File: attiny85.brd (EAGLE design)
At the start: 88.3 x 50.2 mm, 9 parts, among them U2 ATTINY85V-10SU

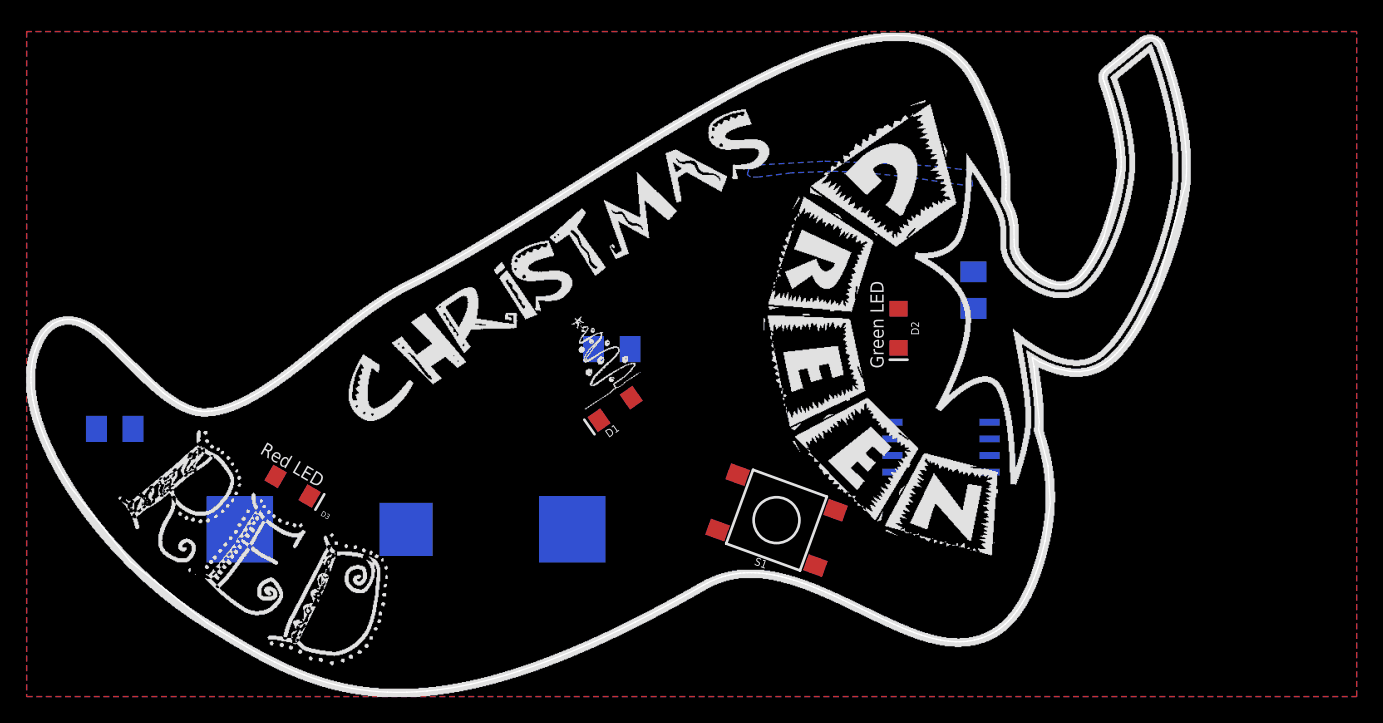
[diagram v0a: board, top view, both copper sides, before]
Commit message: Updating pads and rerouting
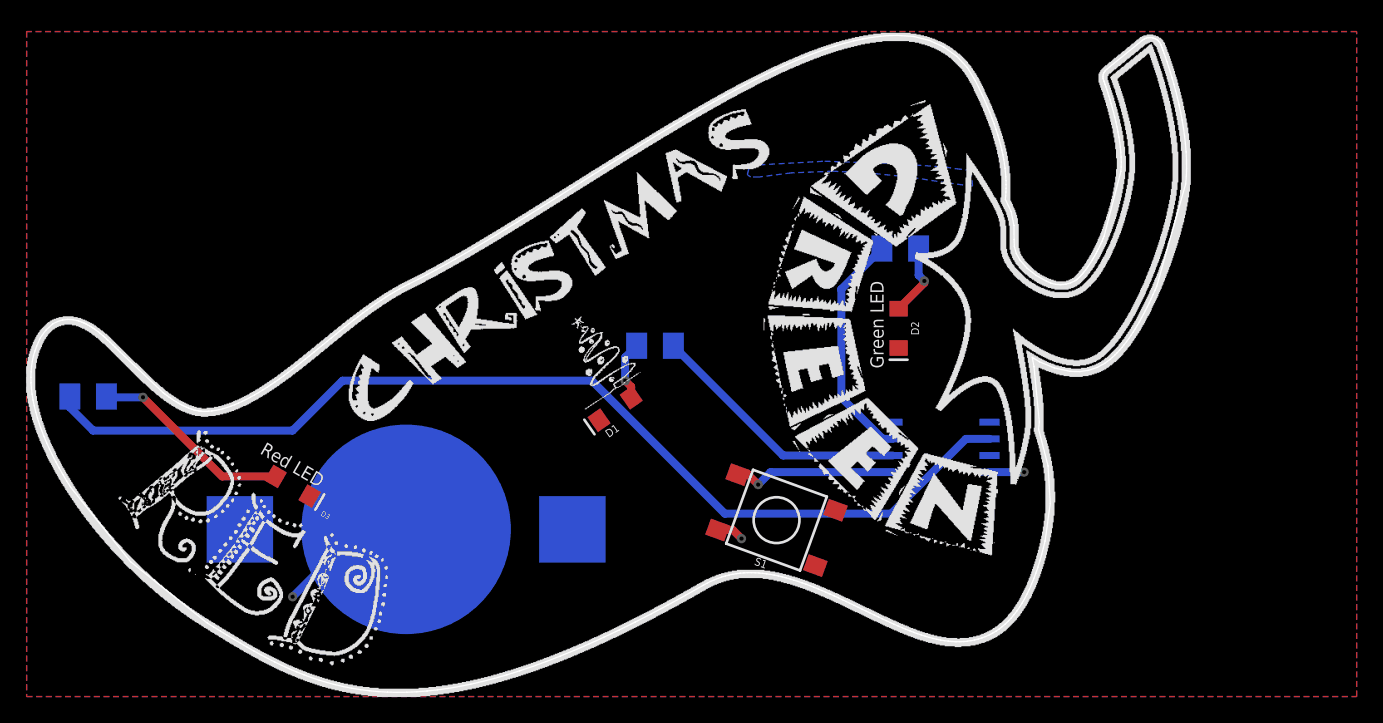
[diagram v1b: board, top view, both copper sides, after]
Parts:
- BAT1: device adafruit:CR2032-SMD -> adafruit-john modded:CR2032-SMD
- moved R2 6.43 mm to (66.7, 34.2), turned to 180 degrees
- moved R1 3.31 mm to (48.0, 26.8), turned to 0 degrees
- moved R3 3.20 mm to (4.70, 22.9)
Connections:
- removed net N$3: BAT1.+$1, BAT1.+$2, S1.B2, U2.8
- new net VCC: BAT1.+$1, BAT1.+$2, S1.B2, U2.8
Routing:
- net N$8: track 0.00 -> 80.0 mm
- net N$4: track 0.00 -> 20.2 mm
- net N$7: track 0.00 -> 17.9 mm
- net N$1: track 0.00 -> 15.5 mm, vias 0 -> 1
- net GND: track 0.00 -> 13.4 mm, vias 0 -> 2
- net N$6: track 0.00 -> 12.5 mm, vias 0 -> 1
- net N$2: track 0.00 -> 5.59 mm, vias 0 -> 1
- net N$5: track 0.00 -> 4.53 mm, vias 0 -> 1
- net VCC: track 0.00 -> 2.10 mm, vias 0 -> 1
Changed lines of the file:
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@@
 <setting verticaltext="up"/>
 </settings>
-<grid distance="0.0025" unitdist="inch" unit="inch" style="lines" multiple="1" display="yes" altdistance="0.0125" altunitdist="inch" altunit="inch"/>
+<grid distance="0.05" unitdist="inch" unit="inch" style="lines" multiple="1" display="yes" altdistance="0.0125" altunitdist="inch" altunit="inch"/>
 <layers>
 <layer number="1" name="Top" color="4" fill="1" visible="yes" active="yes"/>
@@
 </autorouter>
 <elements>
-<element name="R2" library="adafruit" package="M1206" value="1k" x="72.3265" y="31.0515" rot="MR270"/>
+<element name="R2" library="adafruit" package="M1206" value="1k" x="66.7385" y="34.2265" rot="MR180"/>
 <element name="D2" library="SparkFun-LED" package="LED-1206" value="" x="66.6115" y="28.1305" rot="R270"/>
-<element name="R3" library="adafruit" package="M1206" value="1k" x="6.731" y="20.447" rot="MR180"/>
+<element name="R3" library="adafruit" package="M1206" value="1k" x="4.699" y="22.9235" rot="MR180"/>
 <element name="D3" library="SparkFun-LED" package="LED-1206" value="" x="20.32" y="16.0655" smashed="yes" rot="R330">
 <attribute name="NAME" x="22.41786875" y="13.85710625" size="0.4064" layer="25" ratio="10" rot="R330"/>
 <attribute name="VALUE" x="22.1899375" y="12.90351875" size="1.27" layer="27" ratio="10" rot="R330"/>
 </element>
-<element name="BAT1" library="adafruit" package="CR2032-SMD" value="" x="28.9885" y="12.7725" rot="MR0"/>
+<element name="BAT1" library="adafruit-john modded" package="CR2032-SMD" value="" x="28.9885" y="12.7725" rot="MR0"/>
 <element name="U2" library="Atmel_By_element14_Batch_1-00" package="SOIC127P798X216-8N" value="ATTINY85V-10SU" x="69.85" y="19.05" smashed="yes" rot="MR0">
 <attribute name="OC_NEWARK" value="58M3799" x="69.85" y="19.05" size="1.778" layer="28" rot="MR0" display="off"/>
@@
 <attribute name="NAME" x="74.4728" y="13.7922" size="2.0828" layer="26" ratio="10" rot="SMR0"/>
 </element>
-<element name="R1" library="adafruit" package="M1206" value="1k" x="44.704" y="26.543" rot="MR180"/>
+<element name="R1" library="adafruit" package="M1206" value="1k" x="48.006" y="26.797" rot="MR0"/>
 <element name="D1" library="SparkFun-LED" package="LED-1206" value="" x="44.958" y="21.971" smashed="yes" rot="R215">
 <attribute name="NAME" x="44.55183125" y="20.55575625" size="0.6096" layer="25" font="vector" ratio="20" rot="R215" align="bottom-center"/>
@@
 <contactref element="R2" pad="2"/>
 <contactref element="D2" pad="A"/>
-<wire x1="66.6115" y1="29.6305" x2="72.3265" y2="29.6515" width="0" layer="19" extent="1-16"/>
+<wire x1="66.6115" y1="29.6305" x2="68.58" y2="31.599" width="0.6096" layer="1"/>
+<wire x1="68.58" y1="31.599" x2="68.58" y2="31.75" width="0.6096" layer="1"/>
+<via x="68.58" y="31.75" extent="1-16" drill="0.3048"/>
+<wire x1="68.58" y1="31.75" x2="68.1385" y2="32.1915" width="0.6096" layer="16"/>
+<wire x1="68.1385" y1="32.1915" x2="68.1385" y2="34.2265" width="0.6096" layer="16"/>
 </signal>
 <signal name="VCC">
@@
 <vertex x="0" y="50.8"/>
 </polygon>
+<contactref element="BAT1" pad="+$1"/>
+<contactref element="BAT1" pad="+$2"/>
+<contactref element="U2" pad="8"/>
+<contactref element="S1" pad="B2"/>
+<wire x1="52.781228125" y1="12.72185" x2="53.95315" y2="12.72185" width="0.6096" layer="1"/>
+<wire x1="53.95315" y1="12.72185" x2="54.61" y2="12.065" width="0.6096" layer="1"/>
+<via x="54.61" y="12.065" extent="1-16" drill="0.3048"/>
 </signal>
 <signal name="GND">
@@
 <contactref element="D3" pad="C"/>
 <contactref element="D2" pad="C"/>
-<wire x1="73.5584" y1="17.145" x2="66.6115" y2="26.6305" width="0" layer="19" extent="1-16"/>
-<wire x1="43.729271875" y1="21.110634375" x2="66.6115" y2="26.6305" width="0" layer="19" extent="1-1"/>
-<wire x1="28.9885" y1="12.7725" x2="43.729271875" y2="21.110634375" width="0" layer="19" extent="1-16"/>
-<wire x1="21.6190375" y1="15.3155" x2="28.9885" y2="12.7725" width="0" layer="19" extent="1-16"/>
+<wire x1="28.9885" y1="12.7725" x2="25.4725" y2="12.7725" width="0.6096" layer="16"/>
+<wire x1="25.4725" y1="12.7725" x2="20.32" y2="7.62" width="0.6096" layer="16"/>
+<via x="20.32" y="7.62" extent="1-16" drill="0.3048"/>
+<wire x1="73.5584" y1="17.145" x2="76.2" y2="17.145" width="0.6096" layer="16"/>
+<via x="76.2" y="17.145" extent="1-16" drill="0.3048"/>
 </signal>
 <signal name="N$1">
 <contactref element="R3" pad="2"/>
 <contactref element="D3" pad="A"/>
-<wire x1="8.131" y1="20.447" x2="19.020959375" y2="16.8155" width="0" layer="19" extent="1-16"/>
+<wire x1="19.020959375" y1="16.8155" x2="14.9345" y2="16.8155" width="0.6096" layer="1"/>
+<wire x1="14.9345" y1="16.8155" x2="8.89" y2="22.86" width="0.6096" layer="1"/>
+<via x="8.89" y="22.86" extent="1-16" drill="0.3048"/>
+<wire x1="8.89" y1="22.86" x2="6.1625" y2="22.86" width="0.6096" layer="16"/>
+<wire x1="6.1625" y1="22.86" x2="6.099" y2="22.9235" width="0.6096" layer="16"/>
 </signal>
 <signal name="N$5">
 <contactref element="R1" pad="2"/>
 <contactref element="D1" pad="A"/>
-<wire x1="46.186725" y1="22.8313625" x2="46.104" y2="26.543" width="0" layer="19" extent="1-16"/>
+<wire x1="46.606" y1="26.797" x2="45.72" y2="25.911" width="0.6096" layer="16"/>
+<wire x1="45.72" y1="25.911" x2="45.72" y2="24.13" width="0.6096" layer="16"/>
+<via x="45.72" y="24.13" extent="1-16" drill="0.3048"/>
+<wire x1="45.72" y1="24.13" x2="46.186725" y2="23.663275" width="0.6096" layer="1"/>
+<wire x1="46.186725" y1="23.663275" x2="46.186725" y2="22.8313625" width="0.6096" layer="1"/>
 </signal>
 <signal name="NTOUCH">
@@
 </polygon>
 </signal>
-<signal name="N$3">
-<contactref element="BAT1" pad="+$1"/>
-<contactref element="BAT1" pad="+$2"/>
-<contactref element="U2" pad="8"/>
-<contactref element="S1" pad="B2"/>
-<wire x1="52.781228125" y1="12.72185" x2="66.1416" y2="20.955" width="0" layer="19" extent="1-16"/>
-<wire x1="41.6885" y1="12.7725" x2="52.781228125" y2="12.72185" width="0" layer="19" extent="1-16"/>
-<wire x1="16.2885" y1="12.7725" x2="41.6885" y2="12.7725" width="0" layer="19" extent="16-16"/>
-</signal>
 <signal name="N$6">
 <contactref element="U2" pad="5"/>
 <contactref element="S1" pad="A2"/>
-<wire x1="54.32031875" y1="16.95046875" x2="66.1416" y2="17.145" width="0" layer="19" extent="1-16"/>
+<wire x1="66.1416" y1="17.145" x2="56.8325" y2="17.145" width="0.6096" layer="16"/>
+<wire x1="56.8325" y1="17.145" x2="55.88" y2="16.1925" width="0.6096" layer="16"/>
+<via x="55.88" y="16.1925" extent="1-16" drill="0.3048"/>
+<wire x1="55.88" y1="16.1925" x2="55.12203125" y2="16.95046875" width="0.6096" layer="1"/>
+<wire x1="55.12203125" y1="16.95046875" x2="54.32031875" y2="16.95046875" width="0.6096" layer="1"/>
 </signal>
 <signal name="N$4">
 <contactref element="U2" pad="6"/>
 <contactref element="R1" pad="1"/>
-<wire x1="43.304" y1="26.543" x2="66.1416" y2="18.415" width="0" layer="19" extent="16-16"/>
+<wire x1="49.406" y1="26.797" x2="57.788" y2="18.415" width="0.6096" layer="16"/>
+<wire x1="57.788" y1="18.415" x2="66.1416" y2="18.415" width="0.6096" layer="16"/>
 </signal>
 <signal name="N$7">
 <contactref element="U2" pad="7"/>
 <contactref element="R2" pad="1"/>
-<wire x1="66.1416" y1="19.685" x2="72.3265" y2="32.4515" width="0" layer="19" extent="16-16"/>
+<wire x1="65.3385" y1="34.2265" x2="62.23" y2="31.118" width="0.6096" layer="16"/>
+<wire x1="62.23" y1="31.118" x2="62.23" y2="22.86" width="0.6096" layer="16"/>
+<wire x1="62.23" y1="22.86" x2="65.405" y2="19.685" width="0.6096" layer="16"/>
+<wire x1="65.405" y1="19.685" x2="66.1416" y2="19.685" width="0.6096" layer="16"/>
 </signal>
 <signal name="N$8">
 <contactref element="U2" pad="2"/>
 <contactref element="R3" pad="1"/>
-<wire x1="5.331" y1="20.447" x2="73.5584" y2="19.685" width="0" layer="19" extent="16-16"/>
+<wire x1="3.299" y1="22.9235" x2="3.299" y2="22.101" width="0.6096" layer="16"/>
+<wire x1="3.299" y1="22.101" x2="5.08" y2="20.32" width="0.6096" layer="16"/>
+<wire x1="5.08" y1="20.32" x2="20.32" y2="20.32" width="0.6096" layer="16"/>
+<wire x1="20.32" y1="20.32" x2="24.13" y2="24.13" width="0.6096" layer="16"/>
+<wire x1="24.13" y1="24.13" x2="43.18" y2="24.13" width="0.6096" layer="16"/>
+<wire x1="43.18" y1="24.13" x2="53.34" y2="13.97" width="0.6096" layer="16"/>
+<wire x1="53.34" y1="13.97" x2="66.04" y2="13.97" width="0.6096" layer="16"/>
+<wire x1="66.04" y1="13.97" x2="71.755" y2="19.685" width="0.6096" layer="16"/>
+<wire x1="71.755" y1="19.685" x2="73.5584" y2="19.685" width="0.6096" layer="16"/>
 </signal>
 </signals>

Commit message: Updating the board and schematic
This is a fairly big set of changes based on the prototype, going
to run another round just to be sure since I've got enough time.
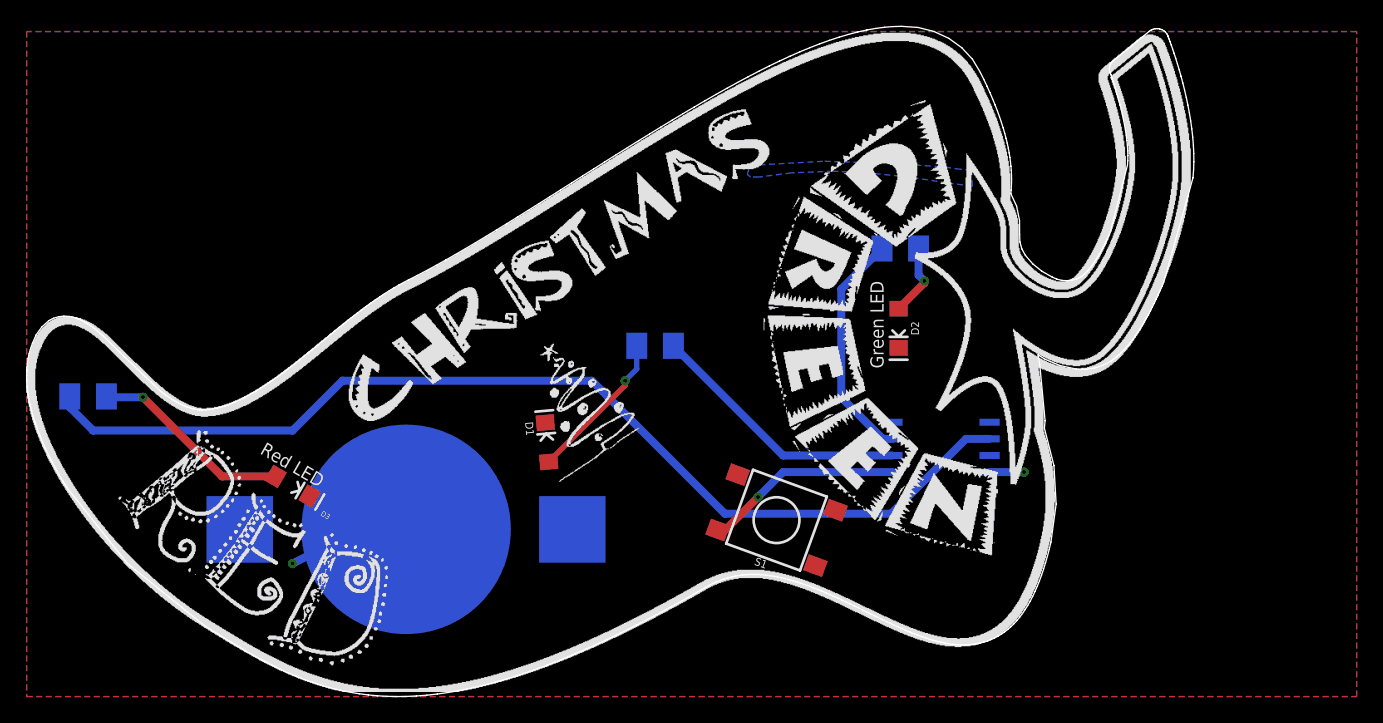
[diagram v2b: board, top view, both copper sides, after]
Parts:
- moved D1 5.79 mm to (39.8, 19.4), turned to 95 degrees
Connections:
- removed net N$6: S1.A2, U2.5
- new net N$3: S1.B2, U2.5
- net GND: now also S1.A2
- net VCC: no longer S1.B2
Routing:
- net N$3: track 0.00 -> 15.2 mm, vias 0 -> 1
- net N$6: track 12.5 -> 0.00 mm, vias 1 -> 0
- net N$5: track 4.53 -> 11.6 mm
- net VCC: track 2.10 -> 0.00 mm, vias 1 -> 0
- net GND: track 13.4 -> 11.9 mm
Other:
- board size 88.3 x 50.2 mm -> 89.2 x 51.2 mm

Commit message: Switching to using the "3" PWMs for the LEDs
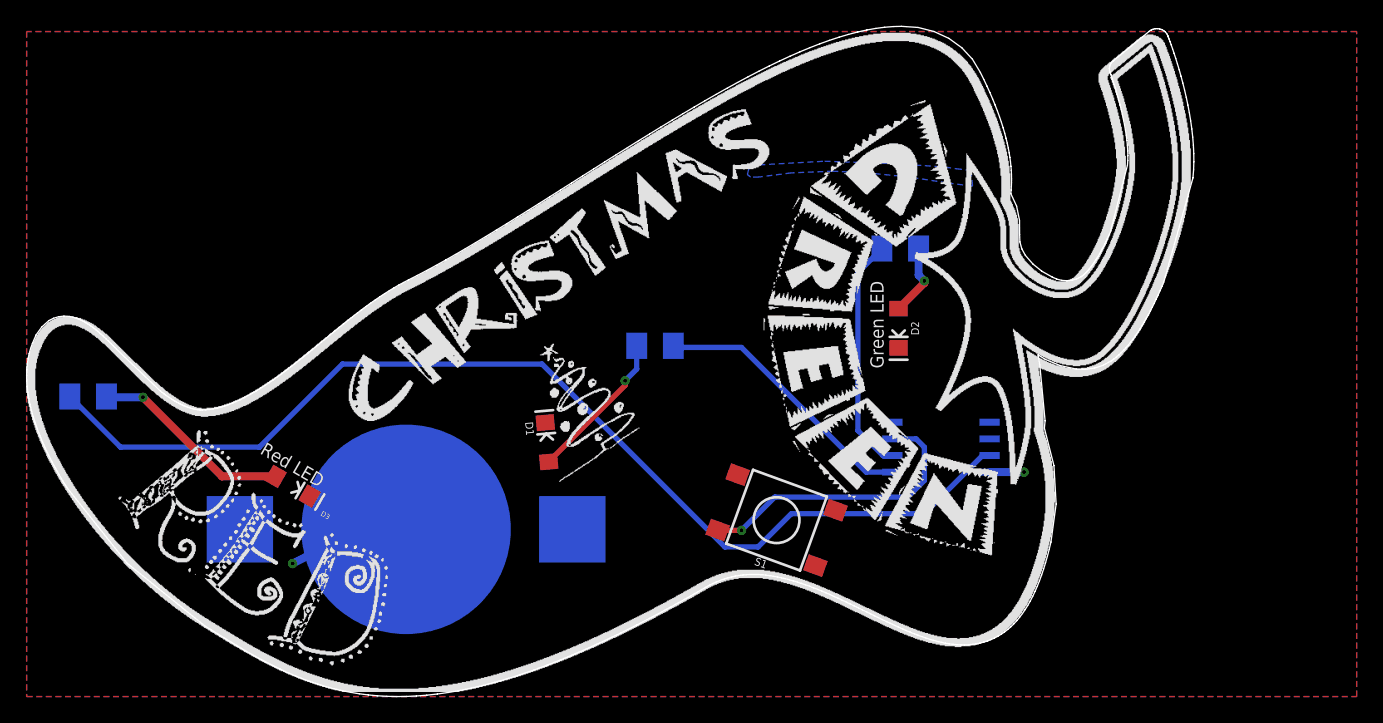
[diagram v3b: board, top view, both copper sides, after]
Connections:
- removed net N$8: R3.1, U2.2
- new net N$6: R3.1, U2.3
- net N$3: now also R1.1; no longer S1.B2
- net N$4: now also R2.1; no longer R1.1
- net N$7: now also S1.B2; no longer R2.1
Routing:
- net N$6: track 0.00 -> 83.2 mm
- net N$8: track 80.0 -> 0.00 mm
- net N$3: track 15.2 -> 20.7 mm, vias 1 -> 0
- net N$7: track 17.9 -> 22.6 mm, vias 0 -> 1
- net N$4: track 20.2 -> 18.1 mm
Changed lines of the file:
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@@
 </polygon>
+</signal>
+<signal name="N$6">
+<contactref element="U2" pad="3"/>
+<contactref element="R3" pad="1"/>
+<wire x1="73.5584" y1="18.415" x2="73.025" y2="18.415" width="0.4064" layer="16"/>
+<wire x1="73.025" y1="18.415" x2="68.58" y2="13.97" width="0.4064" layer="16"/>
+<wire x1="68.58" y1="13.97" x2="58.42" y2="13.97" width="0.4064" layer="16"/>
+<wire x1="58.42" y1="13.97" x2="55.88" y2="11.43" width="0.4064" layer="16"/>
+<wire x1="55.88" y1="11.43" x2="53.34" y2="11.43" width="0.4064" layer="16"/>
+<wire x1="53.34" y1="11.43" x2="39.37" y2="25.4" width="0.4064" layer="16"/>
+<wire x1="39.37" y1="25.4" x2="24.13" y2="25.4" width="0.4064" layer="16"/>
+<wire x1="24.13" y1="25.4" x2="17.78" y2="19.05" width="0.4064" layer="16"/>
+<wire x1="17.78" y1="19.05" x2="7.1725" y2="19.05" width="0.4064" layer="16"/>
+<wire x1="7.1725" y1="19.05" x2="3.299" y2="22.9235" width="0.4064" layer="16"/>
+</signal>
+<signal name="N$3">
+<contactref element="U2" pad="5"/>
+<contactref element="R1" pad="1"/>
+<wire x1="54.61" y1="26.67" x2="49.533" y2="26.67" width="0.4064" layer="16"/>
+<wire x1="49.533" y1="26.67" x2="49.406" y2="26.797" width="0.4064" layer="16"/>
+<wire x1="66.1416" y1="17.145" x2="64.135" y2="17.145" width="0.4064" layer="16"/>
+<wire x1="64.135" y1="17.145" x2="54.61" y2="26.67" width="0.4064" layer="16"/>
 </signal>
 <signal name="N$4">
 <contactref element="U2" pad="6"/>
-<contactref element="R1" pad="1"/>
-<wire x1="49.406" y1="26.797" x2="57.788" y2="18.415" width="0.6096" layer="16"/>
-<wire x1="57.788" y1="18.415" x2="66.1416" y2="18.415" width="0.6096" layer="16"/>
+<contactref element="R2" pad="1"/>
+<wire x1="66.1416" y1="18.415" x2="65.405" y2="18.415" width="0.4064" layer="16"/>
+<wire x1="65.405" y1="18.415" x2="63.5" y2="20.32" width="0.4064" layer="16"/>
+<wire x1="63.5" y1="20.32" x2="63.5" y2="32.388" width="0.4064" layer="16"/>
+<wire x1="63.5" y1="32.388" x2="65.3385" y2="34.2265" width="0.4064" layer="16"/>
 </signal>
 <signal name="N$7">
 <contactref element="U2" pad="7"/>
-<contactref element="R2" pad="1"/>
-<wire x1="65.3385" y1="34.2265" x2="62.23" y2="31.118" width="0.6096" layer="16"/>
-<wire x1="62.23" y1="31.118" x2="62.23" y2="22.86" width="0.6096" layer="16"/>
-<wire x1="62.23" y1="22.86" x2="65.405" y2="19.685" width="0.6096" layer="16"/>
-<wire x1="65.405" y1="19.685" x2="66.1416" y2="19.685" width="0.6096" layer="16"/>
-</signal>
-<signal name="N$8">
-<contactref element="U2" pad="2"/>
-<contactref element="R3" pad="1"/>
-<wire x1="3.299" y1="22.9235" x2="3.299" y2="22.101" width="0.6096" layer="16"/>
-<wire x1="3.299" y1="22.101" x2="5.08" y2="20.32" width="0.6096" layer="16"/>
-<wire x1="5.08" y1="20.32" x2="20.32" y2="20.32" width="0.6096" layer="16"/>
-<wire x1="20.32" y1="20.32" x2="24.13" y2="24.13" width="0.6096" layer="16"/>
-<wire x1="24.13" y1="24.13" x2="43.18" y2="24.13" width="0.6096" layer="16"/>
-<wire x1="43.18" y1="24.13" x2="53.34" y2="13.97" width="0.6096" layer="16"/>
-<wire x1="53.34" y1="13.97" x2="66.04" y2="13.97" width="0.6096" layer="16"/>
-<wire x1="66.04" y1="13.97" x2="71.755" y2="19.685" width="0.6096" layer="16"/>
-<wire x1="71.755" y1="19.685" x2="73.5584" y2="19.685" width="0.6096" layer="16"/>
-</signal>
-<signal name="N$3">
-<contactref element="U2" pad="5"/>
 <contactref element="S1" pad="B2"/>
-<wire x1="66.1416" y1="17.145" x2="57.785" y2="17.145" width="0.6096" layer="16"/>
-<wire x1="57.785" y1="17.145" x2="55.88" y2="15.24" width="0.6096" layer="16"/>
-<via x="55.88" y="15.24" extent="1-16" drill="0.3048"/>
-<wire x1="55.88" y1="15.24" x2="53.36185" y2="12.72185" width="0.6096" layer="1"/>
-<wire x1="53.36185" y1="12.72185" x2="52.781228125" y2="12.72185" width="0.6096" layer="1"/>
+<wire x1="66.1416" y1="19.685" x2="67.945" y2="19.685" width="0.4064" layer="16"/>
+<wire x1="67.945" y1="19.685" x2="68.58" y2="19.05" width="0.4064" layer="16"/>
+<wire x1="68.58" y1="19.05" x2="68.58" y2="16.51" width="0.4064" layer="16"/>
+<wire x1="68.58" y1="16.51" x2="67.31" y2="15.24" width="0.4064" layer="16"/>
+<wire x1="67.31" y1="15.24" x2="57.15" y2="15.24" width="0.4064" layer="16"/>
+<wire x1="57.15" y1="15.24" x2="54.61" y2="12.7" width="0.4064" layer="16"/>
+<via x="54.61" y="12.7" extent="1-16" drill="0.3048"/>
+<wire x1="54.61" y1="12.7" x2="52.803078125" y2="12.7" width="0.4064" layer="1"/>
+<wire x1="52.803078125" y1="12.7" x2="52.781228125" y2="12.72185" width="0.4064" layer="1"/>
 </signal>
 </signals>
